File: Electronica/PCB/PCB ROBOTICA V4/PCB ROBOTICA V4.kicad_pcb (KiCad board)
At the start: 2 copper layers, 79.2 x 139.1 mm, 18 parts, among them J1 Ultrasonico 1, J2 Screw_Terminal_01x02, J3 Ultrasonico 2, J4 Ultrasonico 3, J5 Conn_02x05_Counter_Clockwise, J6 Screw_Terminal_01x02

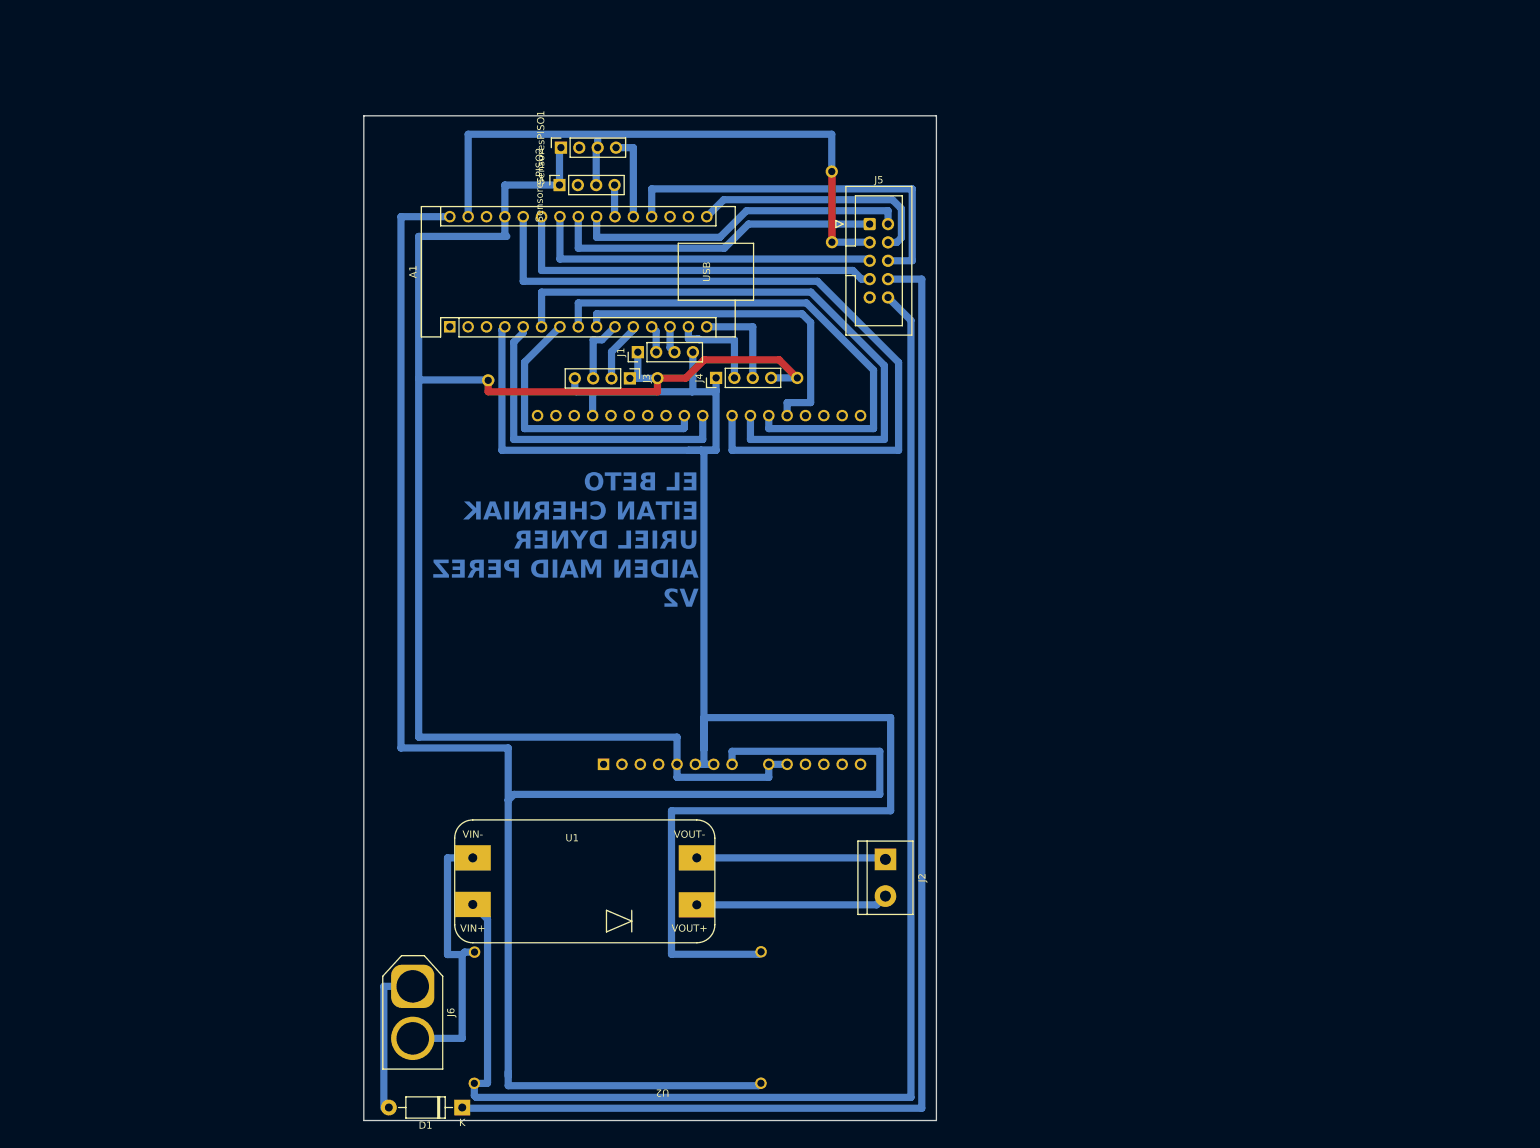
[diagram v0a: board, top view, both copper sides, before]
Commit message: Esquematico PCB V4 terminado
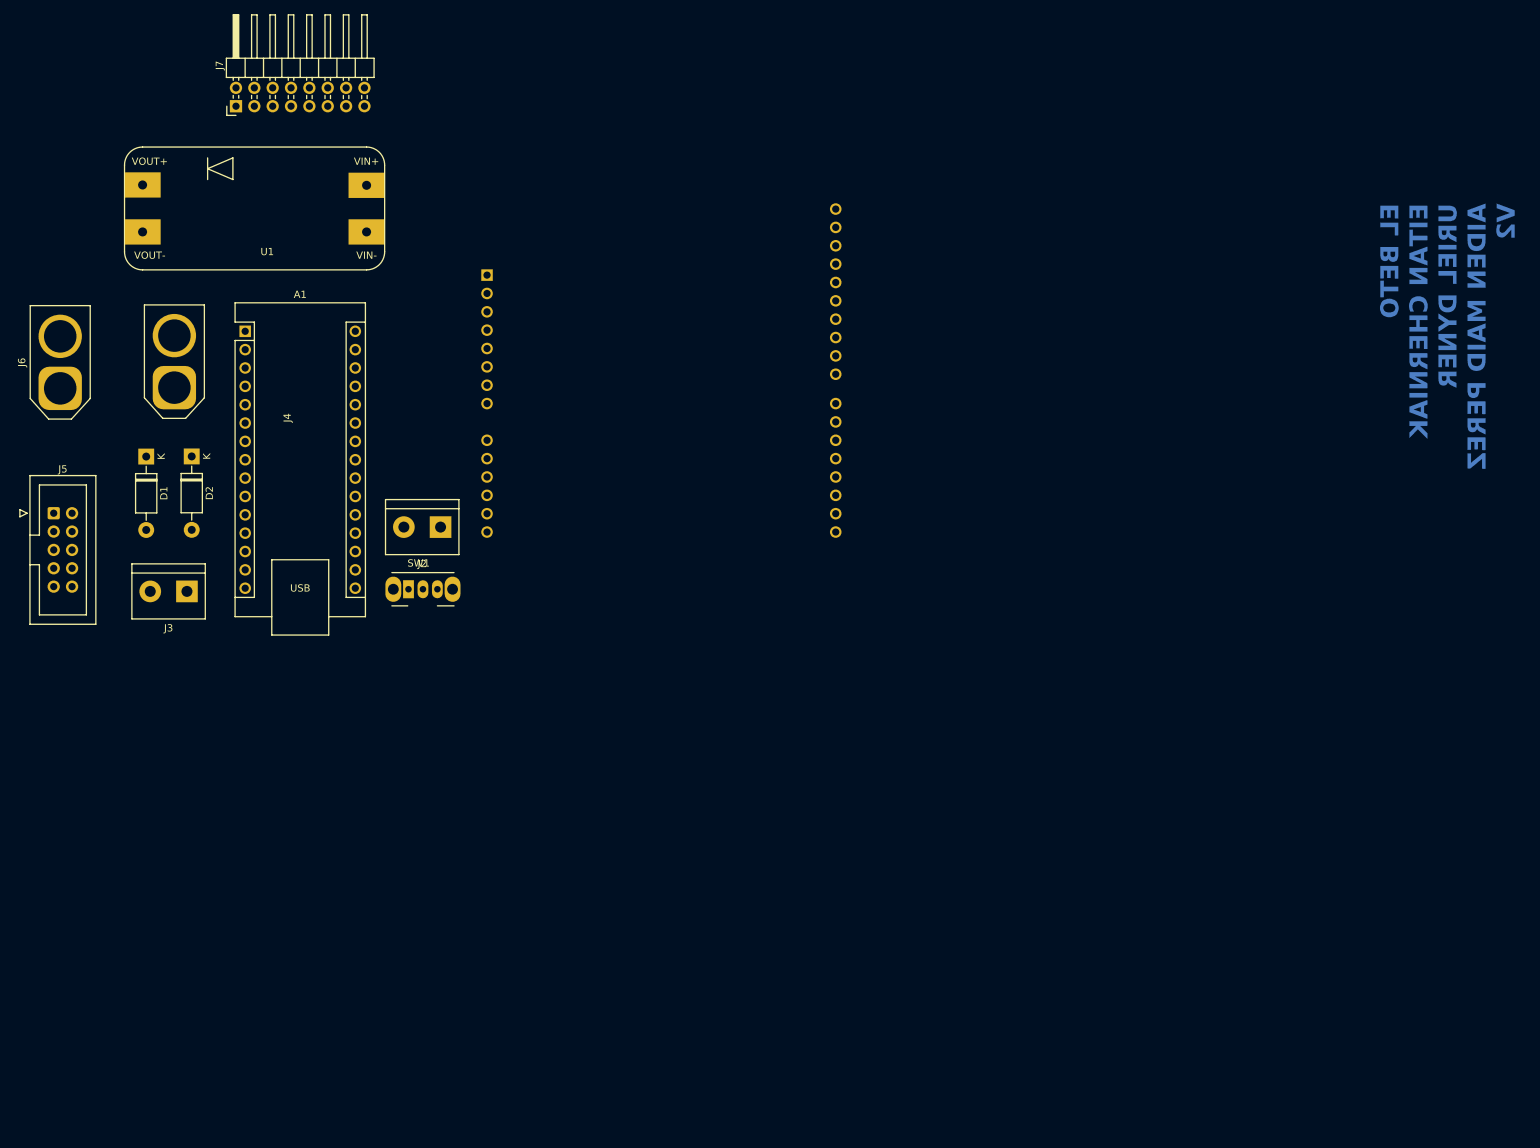
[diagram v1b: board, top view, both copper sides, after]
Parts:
- removed ? (x5): , 
- removed J1: Ultrasonico 1, Connector_PinHeader_2.54mm:PinHeader_1x04_P2.54mm_Vertical
- removed SensoresPISO1, SensoresPISO2: Conn_01x04, Connector_PinSocket_2.54mm:PinSocket_1x04_P2.54mm_Vertical
- removed U2: ~, Step Down:Step Down
- added D2: 1N4007, Diode_THT:D_DO-41_SOD81_P10.16mm_Horizontal, F.Cu at (90.0, 67.4)
- added J7: Conexion Sensores, Connector_PinHeader_2.54mm:PinHeader_2x08_P2.54mm_Horizontal, F.Cu at (96.1, 18.9)
- added SW1: On/Off Motores, Button_Switch_THT:SW_Slide_SPDT_Angled_CK_OS102011MA1Q, F.Cu at (120.0, 85.8)
- J2: value Screw_Terminal_01x02 -> Power Monster
- J3: value Ultrasonico 2 -> On/Off General; footprint Connector_PinHeader_2.54mm:PinHeader_1x04_P2.54mm_Vertical -> TerminalBlock:TerminalBlock_bornier-2_P5.08mm
- J4: value Ultrasonico 3 -> Power Input 2; footprint Connector_PinHeader_2.54mm:PinHeader_1x04_P2.54mm_Vertical -> Connector_AMASS:AMASS_XT60-M_1x02_P7.20mm_Vertical
- J5: value Conn_02x05_Counter_Clockwise -> IDC Placa Botones
- J6: value Screw_Terminal_01x02 -> Power Input 1
- moved J5 119.8 mm to (70.9, 75.3)
- moved U1 102.5 mm to (100.2, 33.1), turned to 0 degrees
- moved D1 100.1 mm to (83.7, 67.4), turned to -90 degrees
- moved J6 96.1 mm to (71.8, 58.0), turned to 90 degrees
- moved J2 76.9 mm to (124.4, 77.2), turned to 180 degrees
- moved J4 75.0 mm to (87.6, 57.9)
- moved A2 69.6 mm to (130.9, 42.3), turned to -90 degrees
- moved J3 68.0 mm to (89.3, 86.1), turned to 180 degrees
- moved A1 28.3 mm to (97.4, 50.1), turned to 0 degrees
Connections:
- A1 pad 16: LED3 -> LED4
- A1 pad 19: LED4 -> LED3
- A1 pad 20: SENSOR DE PISO 1 -> CNY 1
- A1 pad 21: SENSOR DE PISO 2 -> CNY 2
- A1 pad 24: BTN2 -> AIN1 MONSTER SHIELD
- A1 pad 26: AIN1 MONSTER SHIELD -> BTN2
- D1 pad 1: SALIDA V BOTONES -> Net-(D1-K)
- J2 pad 1: Net-(J2-Pin_1) -> GND
- J3 pad 1: +5V -> MOTORES
- J3 pad 2: TRIG 2 -> Net-(D1-K)
- J4 pad 1: GND -> Net-(D1-A)
- J4 pad 2: ECHO 3 -> GND
- J5 pad 10: Entroda V Botones -> unconnected-(J5-Pin_10-Pad10)
- J5 pad 8: SALIDA V BOTONES -> unconnected-(J5-Pin_8-Pad8)
- J6 pad 2: Earth -> GND
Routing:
- net GND: track 330.7 -> 0.00 mm
- net VIN: track 257.6 -> 0.00 mm
- net +5V: track 230.0 -> 0.00 mm
- net Entroda V Botones: track 201.7 -> 0.00 mm
- net SALIDA V BOTONES: track 183.1 -> 0.00 mm
- net AIN1 MONSTER SHIELD: track 105.5 -> 0.00 mm
- net PWM B MONSTER SHIELD: track 88.5 -> 0.00 mm
- net PWM A MONSTER SHIELD: track 72.4 -> 0.00 mm
- net BTN1: track 53.3 -> 0.00 mm
- net LED4: track 53.2 -> 0.00 mm
- net BTN2: track 48.8 -> 0.00 mm
- net BIN 1 MONSTER SHIELD: track 48.1 -> 0.00 mm
- net LED2: track 46.6 -> 0.00 mm
- net LED1: track 46.1 -> 0.00 mm
- net AIN2 MONSTER SHIELD: track 45.6 -> 0.00 mm
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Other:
- board outline removed
